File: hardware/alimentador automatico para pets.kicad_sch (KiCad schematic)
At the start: 1 part, among them U1 ESP32-DEVKIT-V1

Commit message: Added all symbols closed #3
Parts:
- added C?: 100n, symbol Device:C
- added C?: 220u, symbol Device:C_Polarized
- added D?: LED, symbol Device:LED
- added F?: Fuse, symbol Device:Fuse
- added J? (x2): Conn_01x03, symbol Connector_Generic:Conn_01x03
- added J? (x3): Conn_01x02, symbol Connector_Generic:Conn_01x02
- added J? (x2): Conn_01x04, symbol Connector_Generic:Conn_01x04
- added J?: Conn_01x05, symbol Connector_Generic:Conn_01x05
- added PS?: HLK-PM01 5V, Converter_ACDC:Converter_ACDC_HiLink_HLK-PMxx, symbol Converter_ACDC:HLK-PM01
- added R? (x2): 470, symbol Device:R
- added U?: HX711_module, symbol symbol_lib:HX711_module
- U1: footprint ESP32-DEVKIT-V1-footprint:MODULE_ESP32_DEVKIT_V1 -> MODULE_ESP32_DEVKIT_V1
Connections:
- net 3V3: now reaches U1.1 (3V3)
- net 3V3: now also J?.2 (Pin_2), J?.4 (Pin_4), U?.4 (Vcc)
- net sMotor: now reaches U1.10 (D19)
- net sMotor: now also J?.2 (Pin_2)
- net SDA_disp: now reaches U1.11 (D21)
- net SDA_disp: now also J?.2 (Pin_2)
- net SCL_disp: now reaches U1.14 (D22)
- net SCL_disp: now also J?.1 (Pin_1)
- net led_on: now reaches U1.19 (D34)
- net led_on: now also R?.1
- net GND: now reaches U1.2 (GND), U1.29 (GND)
- net GND: now also C?.2, C?.2, D?.1 (K), J?.2 (Pin_2), J?.3 (Pin_3), J?.3 (Pin_3), J?.4 (Pin_4), J?.5 (Pin_5), PS?.3 (-Vout), U?.1 (GND)
- net SCK: now reaches U1.25 (D27)
- net SCK: now also U?.3 (SCK)
- net DT_encoder: now reaches U1.26 (D14)
- net DT_encoder: now also J?.2 (Pin_2)
- net DT: now reaches U1.27 (D12)
- net DT: now also U?.2 (DT)
- net SW_encoder: now reaches U1.28 (D13)
- net SW_encoder: now also J?.3 (Pin_3)
- net CLK_encoder: now reaches U1.3 (D15)
- net CLK_encoder: now also J?.1 (Pin_1)
- net 5V: now reaches U1.30 (VIN)
- net 5V: now also J?.3 (Pin_3), R?.1
- net IR_out: now reaches U1.4 (D2)
- net IR_out: now also J?.1 (Pin_1)
- new net: J?.1 (Pin_1), R?.2
- new net: F?.1, J?.2 (Pin_2)
- new net: F?.2, J?.1 (Pin_1)
- new net: D?.2 (A), R?.2
- new net +5V: C?.1, C?.1, J?.1 (Pin_1), PS?.4 (+Vout)
- new net N: J?.1 (Pin_1), PS?.2 (AC/N)
- new net Phase: J?.2 (Pin_2), PS?.1 (AC/L)
- new net black_wire: J?.2 (Pin_2), U?.9 (-E)
- new net green_wire: J?.4 (Pin_4), U?.7 (+A)
- new net red_wire: J?.1 (Pin_1), U?.10 (+E)
- new net white_wire: J?.3 (Pin_3), U?.8 (-A)
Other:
- note added: "AC/DC Power"
- note added: "Display connection"
- note added: "ESP32 DEVKIT V1"
- note added: "Led indicator (external)"
- note added: "Led indicator (internal 5V)"
- note added: "Load cell interface HX711"
- note added: "Load sensor"
- note added: "Power force"
- note added: "Presence sensor"
- note added: "Rotary encoder"
- note added: "Servo motor connector"
- company: (none) -> UFSC
- title: (none) -> Alimentador automático para pets

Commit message: add push buttons to shcematic
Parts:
- added R? (x3): 27k, symbol Device:R
- added SW? (x3): SW_Push, symbol Switch:SW_Push
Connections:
- net 3V3: now also R?.1, R?.1, R?.1
- net SW3: now reaches U1.20 (D35)
- net SW3: now also SW?.1
- net SW1: now reaches U1.21 (D32)
- net SW1: now also SW?.1
- net SW2: now reaches U1.22 (D33)
- net SW2: now also SW?.1
- new net: R?.2, SW?.2 (x3)
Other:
- note added: "Push buttons"

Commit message: add references to push buttons and resistors
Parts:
- gave numbers to parts that had none: 22

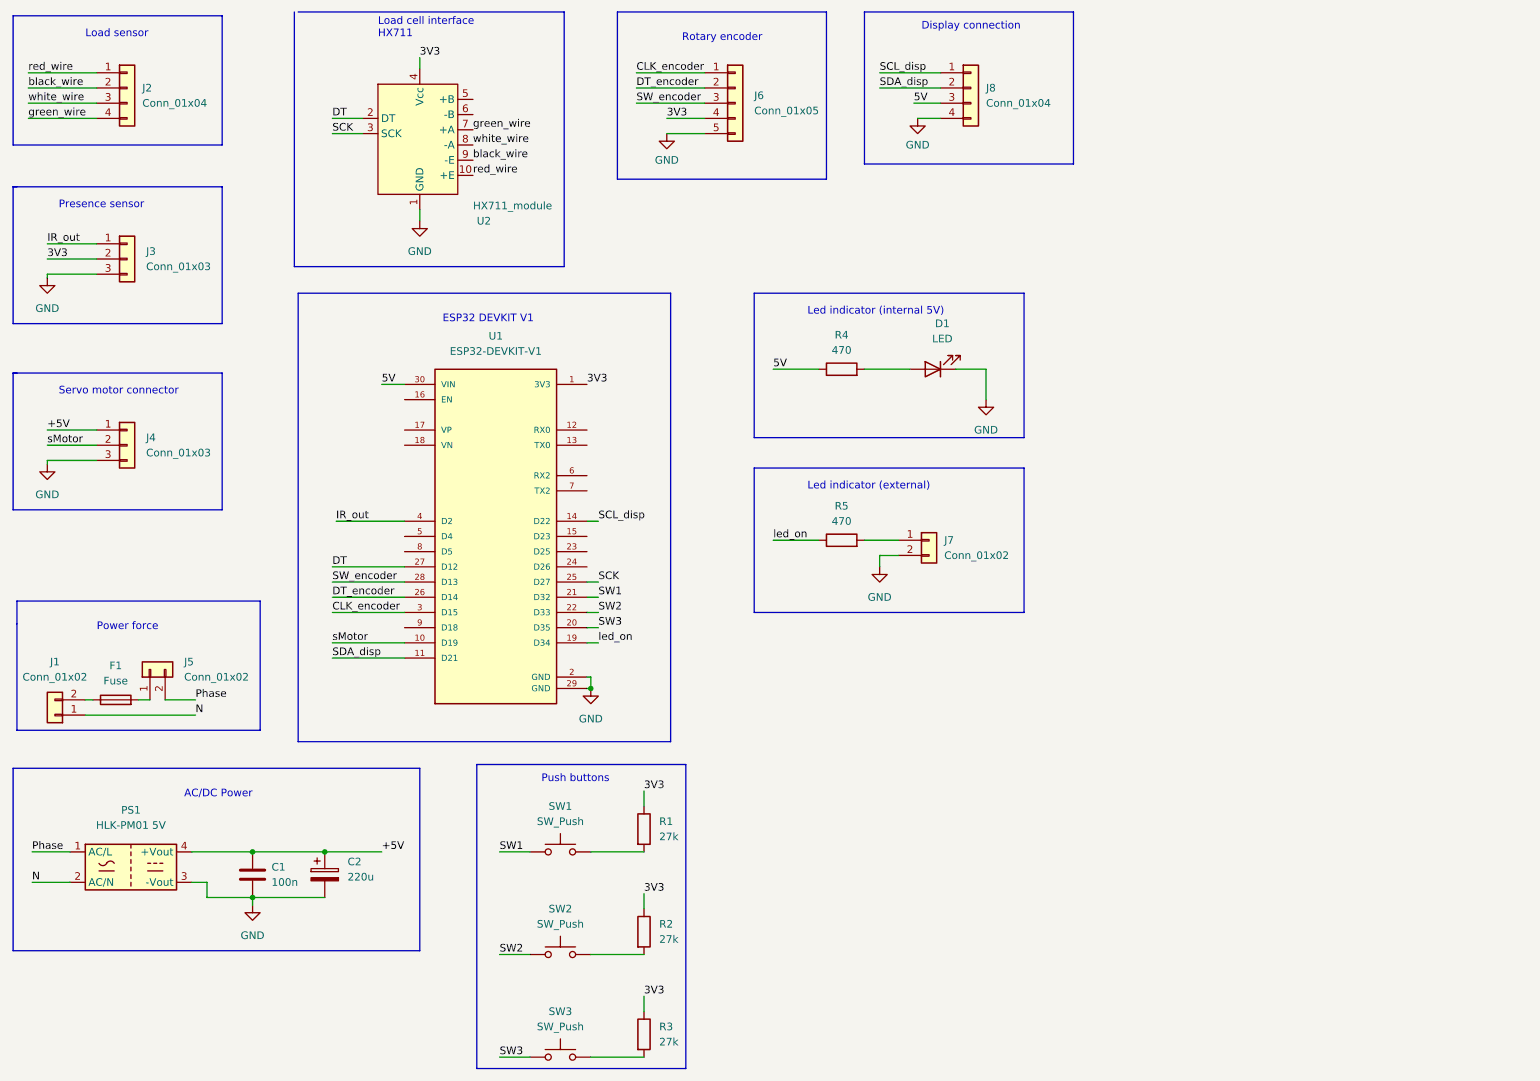
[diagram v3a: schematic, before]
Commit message: Modified presence sensor pin and voltage closed #15
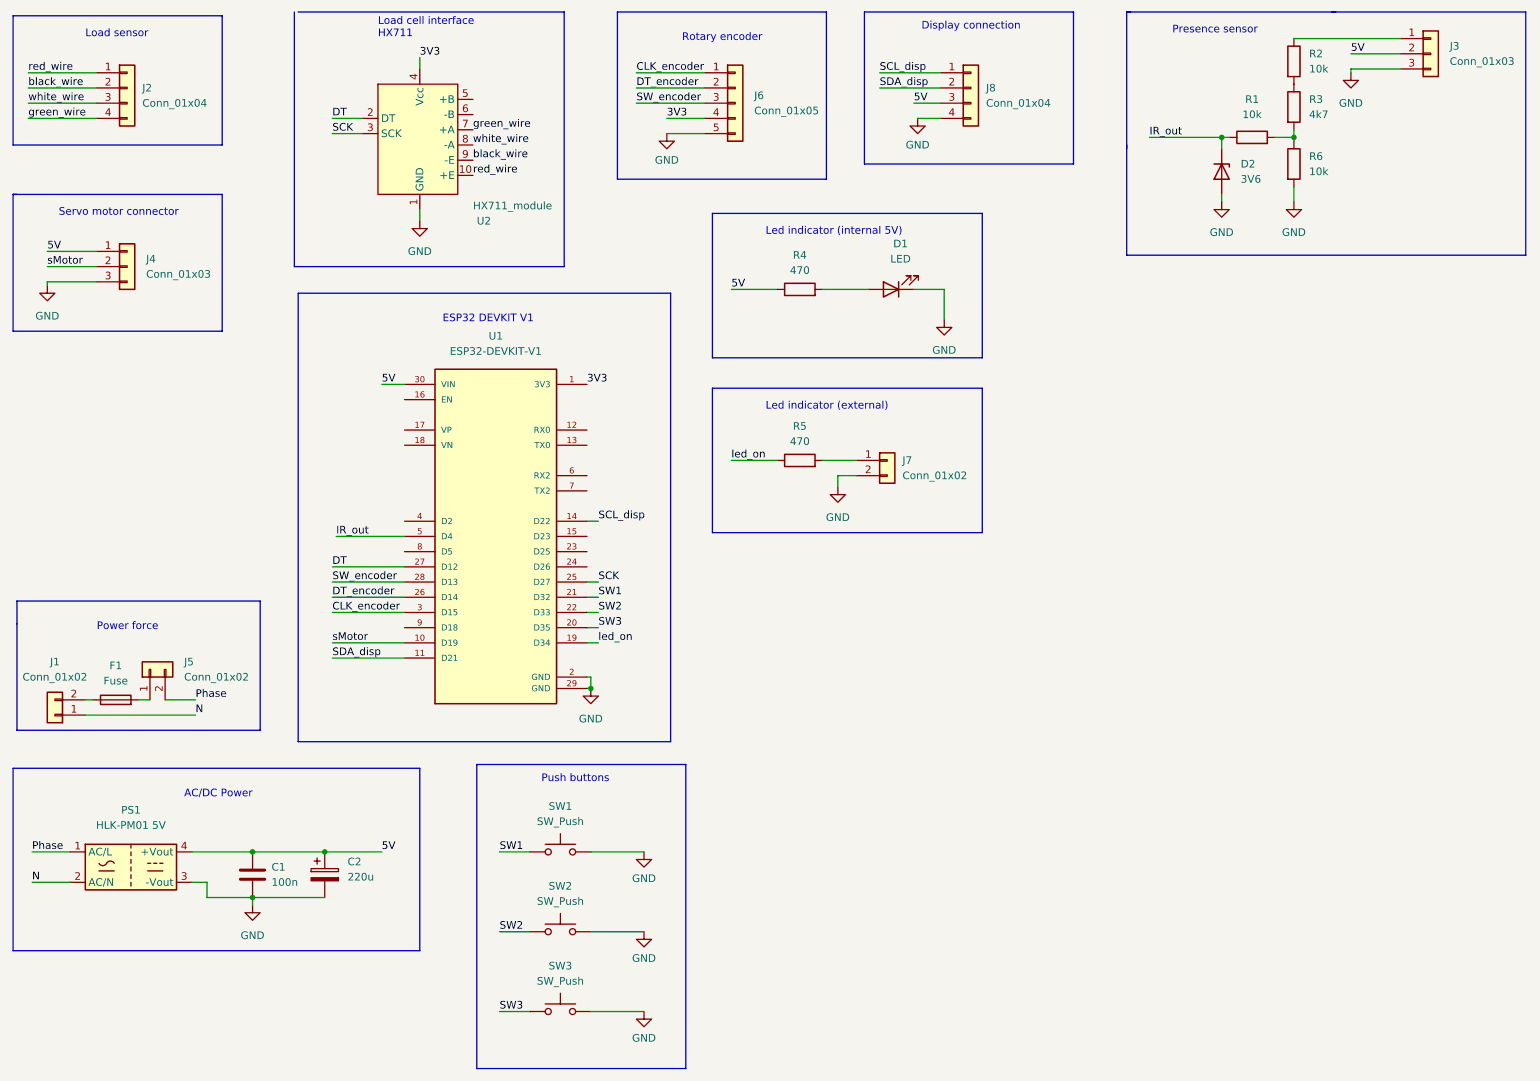
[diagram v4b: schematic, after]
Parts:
- added D2: 3V6, symbol Device:D_Zener
- added R6: 10k, symbol Device:R
- R1, R2: value 27k -> 10k
- R3: value 27k -> 4k7
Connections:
- net +5V is gone; now on net 5V: C1.1, C2.1, J4.1 (Pin_1), PS1.4 (+Vout)
- net 3V3: no longer J3.2 (Pin_2), R1.1, R2.1, R3.1
- net 5V: now also J3.2 (Pin_2)
- net GND: now also SW1.2, SW2.2, SW3.2, D2.2 (A), R6.2
- net IR_out: now also R1.1, U1.5 (D4), D2.1 (K); no longer J3.1 (Pin_1), U1.4 (D2)
- net at R2.2: now also R3.1; no longer SW2.2
- net at R3.2: now also R1.2, R6.1; no longer SW3.2
- new net: J3.1 (Pin_1), R2.1
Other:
- moved on the sheet: D1, J3, J4, J7, R4, R5, SW2, SW3

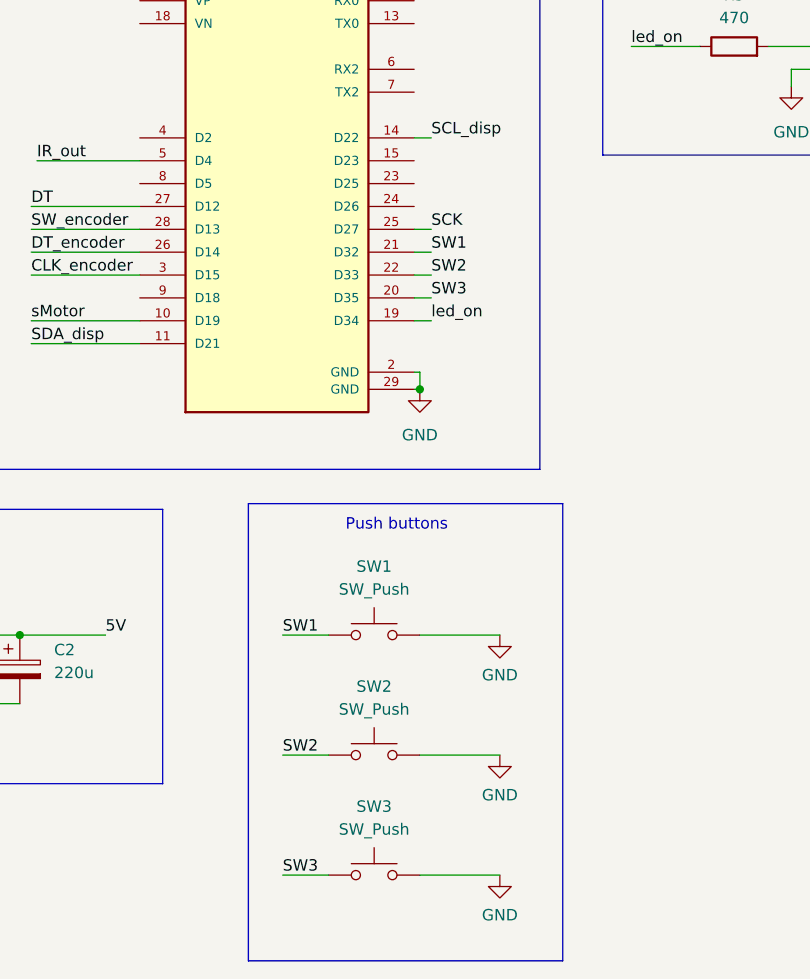
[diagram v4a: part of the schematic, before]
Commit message: change labels and pins for buttons closed #17
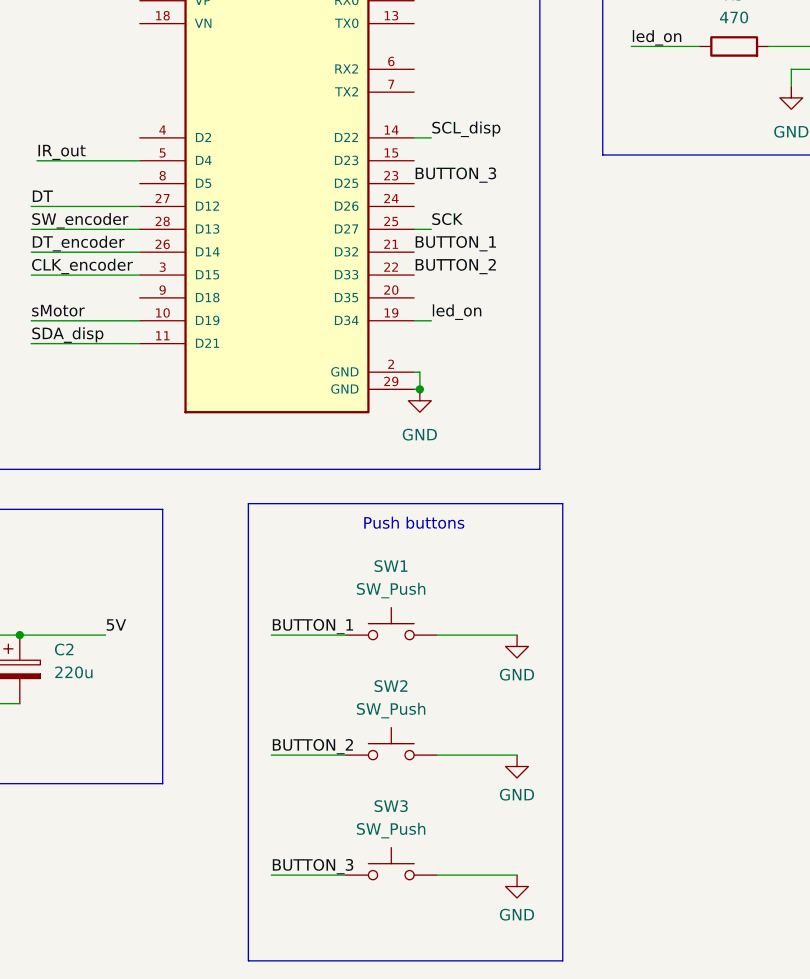
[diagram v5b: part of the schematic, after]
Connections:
- net BUTTON_3: now reaches U1.23 (D25)
- net BUTTON_3: now also SW3.1
- net SW1 renamed BUTTON_1
- net SW2 renamed BUTTON_2
- net SW3: no longer names the net of U1.20 (D35)
- net SW3: no longer SW3.1
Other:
- moved on the sheet: SW1, SW2, SW3

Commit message: rearrange schematic
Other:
- moved on the sheet: C1, C2, D1, D2, F1, J1, J3, J4, J5, J6, J7, J8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

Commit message: pcb design start
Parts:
- removed F1: Fuse, symbol Device:Fuse
- C1: footprint (none) -> Capacitor_THT:C_Disc_D6.0mm_W2.5mm_P5.00mm
- C2: footprint (none) -> Capacitor_THT:CP_Radial_D8.0mm_P2.50mm
- D1: footprint (none) -> LED_THT:LED_D3.0mm
- D2: footprint (none) -> Diode_THT:D_DO-35_SOD27_P7.62mm_Horizontal
- J1, J5, J7: footprint (none) -> Connector_PinSocket_2.54mm:PinSocket_1x02_P2.54mm_Vertical
- J2, J8: footprint (none) -> Connector_PinSocket_2.54mm:PinSocket_1x04_P2.54mm_Vertical
- J3, J4: footprint (none) -> Connector_PinSocket_2.54mm:PinSocket_1x03_P2.54mm_Vertical
- J6: footprint (none) -> Connector_PinSocket_2.54mm:PinSocket_1x05_P2.54mm_Vertical
- R1, R2, R3, R4, R5, R6: footprint (none) -> Resistor_THT:R_Axial_DIN0207_L6.3mm_D2.5mm_P7.62mm_Horizontal
- SW1, SW2, SW3: footprint (none) -> Button_Switch_THT:SW_PUSH_6mm
- U1: footprint MODULE_ESP32_DEVKIT_V1 -> ESP32-DEVKIT-V1-footprint:MODULE_ESP32_DEVKIT_V1
- U2: footprint (none) -> footprint_lib:HX711_module
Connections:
- net at J1.2 (Pin_2): now also J5.1 (Pin_1)
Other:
- note added: "fuse_conn"
